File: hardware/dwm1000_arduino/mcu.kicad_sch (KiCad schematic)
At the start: 3 parts

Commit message: finixh schematic and first pass layout
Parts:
- added TP3: DWM_GPIO7, symbol Connector:TestPoint_Small
- added TP4: DWM_GPIO4, symbol Connector:TestPoint_Small
- R1: footprint (none) -> Resistor_SMD:R_0805_2012Metric_Pad1.20x1.40mm_HandSolder; DigiKey (none) -> RMCF0805JT10K0DKR-ND
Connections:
- net DWM_SPIHA: now also A1.10 (D7); no longer A1.9 (D6)
- net DWM_SPIPOL: now also A1.9 (D6); no longer A1.10 (D7)
- net at DWM1.11 (GPIO4/EXTPA): now also TP4.1
- net at DWM1.4 (GPIO7): now also TP3.1
- no-connect marks 11 -> 9
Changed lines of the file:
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@@
   (junction (at 262.89 156.21) (diameter 0) (color 0 0 0 0)
   )
-  (no_connect (at 288.29 135.89))
   (no_connect (at 151.13 143.51))
   (no_connect (at 151.13 138.43))
@@
   (no_connect (at 151.13 120.65))
   (no_connect (at 151.13 113.03))
-  (no_connect (at 242.57 128.27))
   (no_connect (at 125.73 120.65))
   (no_connect (at 151.13 110.49))
@@
     (stroke (width 0) (type default) (color 0 0 0 0))
   )
+  (wire (pts (xy 288.29 135.89) (xy 302.26 135.89))
+    (stroke (width 0) (type default) (color 0 0 0 0))
+  )
   (wire (pts (xy 135.89 97.79) (xy 135.89 100.33))
     (stroke (width 0) (type default) (color 0 0 0 0))
@@
     (effects (font (size 1.27 1.27)) (justify left bottom))
   )
-  (label "DWM_SPIPOL" (at 125.73 128.27 180)
+  (label "DWM_SPIPOL" (at 125.73 125.73 180)
     (effects (font (size 1.27 1.27)) (justify right bottom))
   )
@@
     (effects (font (size 1.27 1.27)) (justify left bottom))
   )
-  (label "DWM_SPIHA" (at 125.73 125.73 180)
+  (label "DWM_SPIHA" (at 125.73 128.27 180)
     (effects (font (size 1.27 1.27)) (justify right bottom))
   )
@@
     )
   )
-  (symbol (lib_id "power:+3V3") (at 267.97 93.98 0)
+  (symbol (lib_id "Connector:TestPoint_Small") (at 242.57 128.27 0) (unit 1)
+    (in_bom yes) (on_board yes)
+    (property "Reference" "TP3" (id 0) (at 238.76 127 0)
+      (effects (font (size 1.27 1.27)) (justify left))
+    )
+    (property "Value" "DWM_GPIO7" (id 1) (at 231.14 129.54 0)
+      (effects (font (size 1.27 1.27)) (justify left))
+    )
+    (property "Footprint" "" (id 2) (at 247.65 128.27 0)
+      (effects (font (size 1.27 1.27)) hide)
+    )
+    (property "Datasheet" "~" (id 3) (at 247.65 128.27 0)
+      (effects (font (size 1.27 1.27)) hide)
+    )
+    (pin "1")
+  )
+  (symbol (lib_id "power:+3V3") (at 267.97 93.98 0) (unit 1)
     (in_bom yes) (on_board yes) (fields_autoplaced)
     (property "Reference" "#PWR011" (id 0) (at 267.97 97.79 0)
@@
     (pin "1")
   )
-  (symbol (lib_id "power:+3V3") (at 140.97 97.79 0)
+  (symbol (lib_id "power:+3V3") (at 140.97 97.79 0) (unit 1)
     (in_bom yes) (on_board yes)
     (property "Reference" "#PWR07" (id 0) (at 140.97 101.6 0)
@@
     (pin "1")
   )
-  (symbol (lib_id "power:GND") (at 303.53 114.3 0)
+  (symbol (lib_id "power:GND") (at 303.53 114.3 0) (unit 1)
     (in_bom yes) (on_board yes) (fields_autoplaced)
     (property "Reference" "#PWR012" (id 0) (at 303.53 120.65 0)
@@
     (pin "1")
   )
-  (symbol (lib_id "MCU_Module:Arduino_Nano_v2.x") (at 138.43 125.73 0)
+  (symbol (lib_id "MCU_Module:Arduino_Nano_v2.x") (at 138.43 125.73 0) (unit 1)
     (in_bom yes) (on_board yes)
     (property "Reference" "A1" (id 0) (at 128.27 101.6 0)
@@
     (pin "9")
   )
-  (symbol (lib_id "RF_Module:DWM1000") (at 265.43 125.73 0)
+  (symbol (lib_id "RF_Module:DWM1000") (at 265.43 125.73 0) (unit 1)
     (in_bom yes) (on_board yes) (fields_autoplaced)
     (property "Reference" "DWM1" (id 0) (at 269.9894 98.9035 0)
@@
     (pin "9")
   )
-  (symbol (lib_id "power:+5V") (at 143.51 97.79 0)
+  (symbol (lib_id "Connector:TestPoint_Small") (at 302.26 135.89 270) (unit 1)
+    (in_bom yes) (on_board yes) (fields_autoplaced)
+    (property "Reference" "TP4" (id 0) (at 303.403 134.9815 90)
+      (effects (font (size 1.27 1.27)) (justify left))
+    )
+    (property "Value" "DWM_GPIO4" (id 1) (at 303.403 137.7566 90)
+      (effects (font (size 1.27 1.27)) (justify left))
+    )
+    (property "Footprint" "" (id 2) (at 302.26 140.97 0)
+      (effects (font (size 1.27 1.27)) hide)
+    )
+    (property "Datasheet" "~" (id 3) (at 302.26 140.97 0)
+      (effects (font (size 1.27 1.27)) hide)
+    )
+    (pin "1")
+  )
+  (symbol (lib_id "power:+5V") (at 143.51 97.79 0) (unit 1)
     (in_bom yes) (on_board yes)
     (property "Reference" "#PWR08" (id 0) (at 143.51 101.6 0)
@@
     (pin "1")
   )
-  (symbol (lib_id "Device:R_Small") (at 303.53 109.22 0)
+  (symbol (lib_id "Device:R_Small") (at 303.53 109.22 0) (unit 1)
     (in_bom yes) (on_board yes) (fields_autoplaced)
     (property "Reference" "R1" (id 0) (at 305.0286 108.3115 0)
@@
       (effects (font (size 1.27 1.27)) (justify left))
     )
-    (property "Footprint" "" (id 2) (at 303.53 109.22 0)
+    (property "Footprint" "Resistor_SMD:R_0805_2012Metric_Pad1.20x1.40mm_HandSolder" (id 2) (at 303.53 109.22 0)
       (effects (font (size 1.27 1.27)) hide)
     )
@@
       (effects (font (size 1.27 1.27)) hide)
     )
+    (property "DigiKey" "RMCF0805JT10K0DKR-ND" (id 4) (at 303.53 109.22 0)
+      (effects (font (size 1.27 1.27)) hide)
+    )
     (pin "1")
     (pin "2")
   )
-  (symbol (lib_id "power:GND") (at 265.43 160.02 0)
+  (symbol (lib_id "power:GND") (at 265.43 160.02 0) (unit 1)
     (in_bom yes) (on_board yes) (fields_autoplaced)
     (property "Reference" "#PWR010" (id 0) (at 265.43 166.37 0)
@@
     (pin "1")
   )
-  (symbol (lib_id "power:GND") (at 138.43 157.48 0)
+  (symbol (lib_id "power:GND") (at 138.43 157.48 0) (unit 1)
     (in_bom yes) (on_board yes) (fields_autoplaced)
     (property "Reference" "#PWR06" (id 0) (at 138.43 163.83 0)
@@
     (pin "1")
   )
-  (symbol (lib_id "power:+3V3") (at 262.89 93.98 0)
+  (symbol (lib_id "power:+3V3") (at 262.89 93.98 0) (unit 1)
     (in_bom yes) (on_board yes) (fields_autoplaced)
     (property "Reference" "#PWR09" (id 0) (at 262.89 97.79 0)

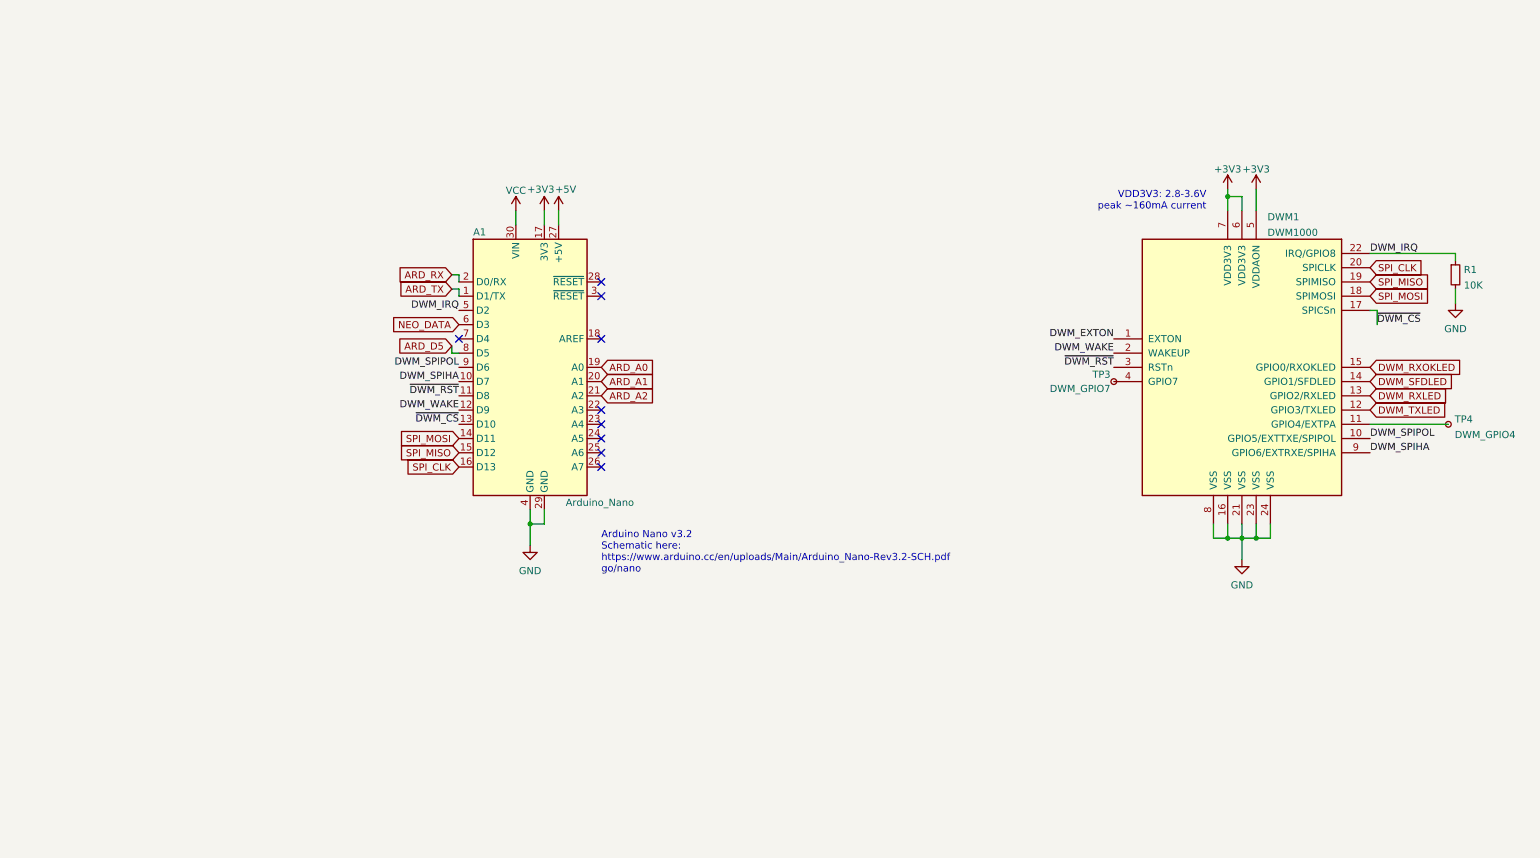
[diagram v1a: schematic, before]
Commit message: start rev 2 of the dwm board
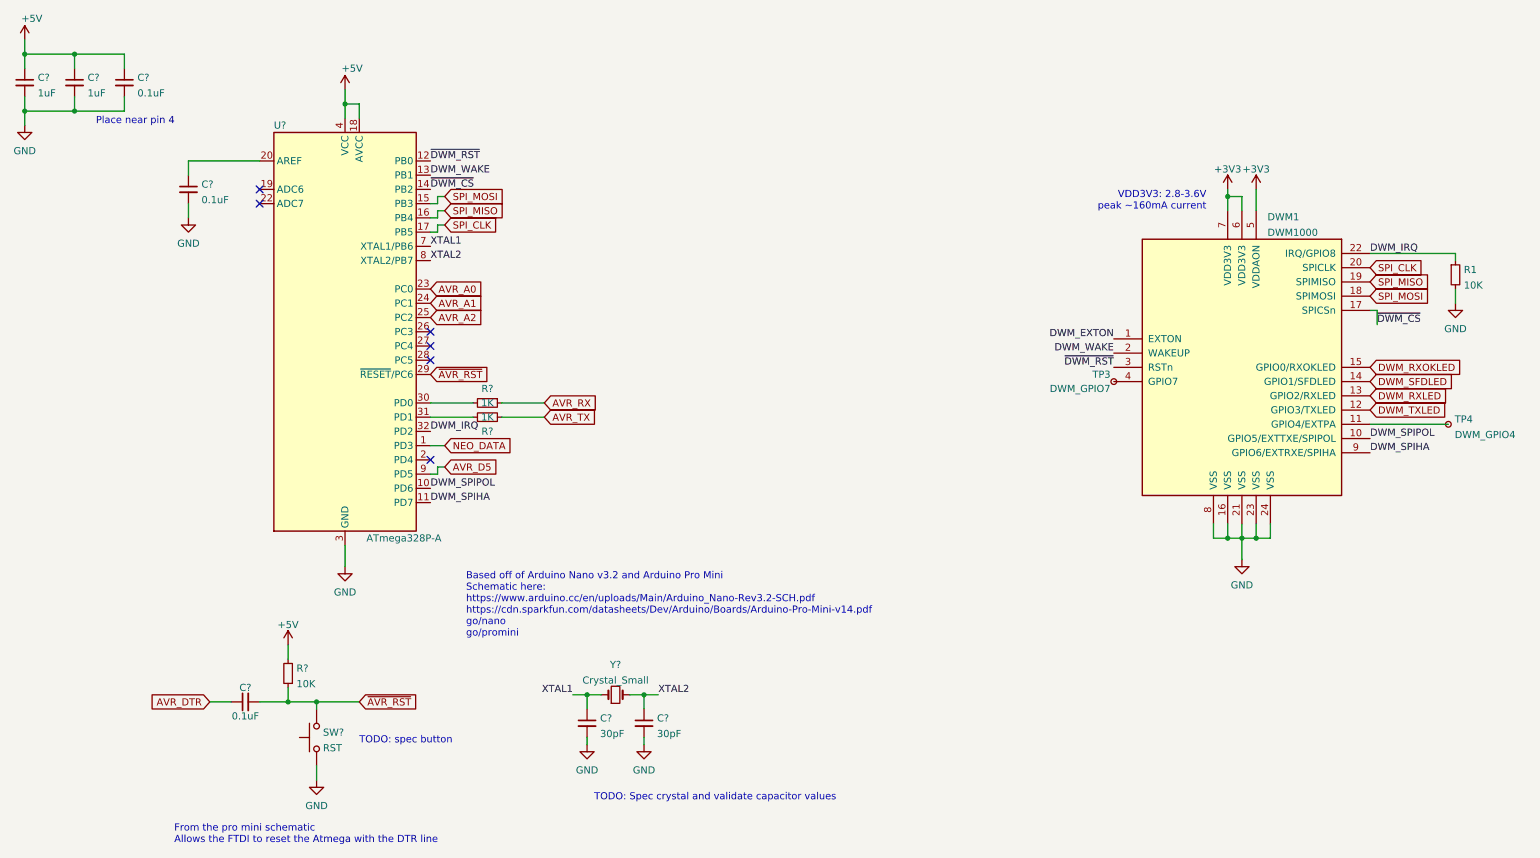
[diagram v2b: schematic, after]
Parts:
- removed A1: Arduino_Nano, Module:Arduino_Nano, symbol MCU_Module:Arduino_Nano_v2.x
- added C? (x2): 1uF, symbol Device:C_Small
- added C? (x3): 0.1uF, symbol Device:C_Small
- added C? (x2): 30pF, symbol Device:C_Small
- added R? (x2): 1K, symbol Device:R_Small
- added R?: 10K, symbol Device:R_Small
- added SW?: RST, symbol Switch:SW_Push
- added U?: ATmega328P-A, Package_QFP:TQFP-32_7x7mm_P0.8mm, symbol MCU_Microchip_ATmega:ATmega328P-A
- added Y?: Crystal_Small, symbol Device:Crystal_Small
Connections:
- net +5V: now also C?.1, C?.1, C?.1, R?.2, U?.18 (AVCC), U?.4 (VCC), U?.6 (VCC)
- net DWM_IRQ: now also U?.32 (PD2)
- net DWM_SPIHA: now also U?.11 (PD7)
- net DWM_SPIPOL: now also U?.10 (PD6)
- net DWM_WAKE: now also U?.13 (PB1)
- net GND: now also C?.2, C?.2, C?.2, C?.2, C?.2, C?.2, SW?.1, U?.21 (GND), U?.3 (GND), U?.5 (GND)
- net NEO_DATA: now also U?.1 (PD3)
- net SPI_CLK: now also U?.17 (PB5)
- net SPI_MISO: now also U?.16 (PB4)
- net SPI_MOSI: now also U?.15 (PB3)
- net ~{DWM_CS}: now also U?.14 (PB2)
- net ~{DWM_RST}: now also U?.12 (PB0)
- new net: R?.2, U?.30 (PD0)
- new net: C?.1, U?.20 (AREF)
- new net: R?.1, U?.31 (PD1)
- new net AVR_A0: U?.23 (PC0)
- new net AVR_A1: U?.24 (PC1)
- new net AVR_A2: U?.25 (PC2)
- new net AVR_D5: U?.9 (PD5)
- new net AVR_DTR: C?.1
- new net AVR_RX: R?.1
- new net AVR_TX: R?.2
- new net XTAL1: C?.1, U?.7 (XTAL1/PB6), Y?.1
- new net XTAL2: C?.1, U?.8 (XTAL2/PB7), Y?.2
- new net ~{AVR_RST}: C?.2, R?.1, SW?.2, U?.29 (~{RESET}/PC6)
- no-connect marks 9 -> 6
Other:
- note added: "Based off of Arduino Nano v3.2 and Arduino Pro Mini Schematic here: https://www.arduino.cc/en/uploads/Main/Arduino_Nano-Rev3.2-SCH.pdf https://cdn.sparkfun.com/datasheets/Dev/Arduino/Boards/Arduino-Pro-Mini-v14.pdf go/nano go/promini"
- note added: "From the pro mini schematic Allows the FTDI to reset the Atmega with the DTR line"
- note added: "Place near pin 4"
- note added: "TODO: Spec crystal and validate capacitor values"
- note added: "TODO: spec button"
- note removed: "Arduino Nano v3.2 Schematic here: https://www.arduino.cc/en/uploads/Main/Arduino_Nano-Rev3.2-SCH.pdf go/nano"

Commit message: rev 2 pcb schematic
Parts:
- added C8: 1uF, symbol Device:C_Small
- R3, R4: renamed from R?; DigiKey (none) -> RMCF0805FT1K00CT-ND
- SW1: renamed from SW?; DigiKey (none) -> CKN12307-ND
- gave numbers to parts that had none: 10
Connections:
- net +3V3: now also C8.1
- net GND: now also C8.2
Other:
- note added: "Place near pin 6"
- moved on the sheet: R3, R4

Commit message: finish layout
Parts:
- removed C6, C7: 30pF, symbol Device:C_Small
- removed TP3: DWM_GPIO7, symbol Connector:TestPoint_Small
- removed TP4: DWM_GPIO4, symbol Connector:TestPoint_Small
- removed Y1: Crystal_Small, symbol Device:Crystal_Small
- C1, C2, C3, C4, C5, C8: footprint (none) -> Capacitor_SMD:C_0805_2012Metric_Pad1.18x1.45mm_HandSolder
- R2, R3, R4: footprint (none) -> Resistor_SMD:R_0805_2012Metric_Pad1.20x1.40mm_HandSolder
- SW1: footprint (none) -> Button_Switch_THT:SW_PUSH_6mm
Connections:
- net DWM_RXLED: no longer names the net of DWM1.13 (GPIO2/RXLED)
- net DWM_RXOKLED: no longer names the net of DWM1.15 (GPIO0/RXOKLED)
- net DWM_SFDLED: no longer names the net of DWM1.14 (GPIO1/SFDLED)
- net DWM_TXLED: no longer names the net of DWM1.12 (GPIO3/TXLED)
- net XTAL1: no longer names the net of U1.7 (XTAL1/PB6)
- net XTAL2: no longer names the net of U1.8 (XTAL2/PB7)
- no-connect marks 6 -> 14
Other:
- note removed: "TODO: Spec crystal and validate capacitor values"
